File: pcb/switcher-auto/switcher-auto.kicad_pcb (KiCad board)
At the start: 2 copper layers, 129 x 81 mm, 9 parts, among them J1 Conn_02x22_Top_Bottom, J2 Conn_02x22_Top_Bottom, J3 Conn_02x22_Top_Bottom, U1 CD74HC4067SM96, U2 CD74HC4067SM96, U3 CD74HC4067SM96, U4 CD74HC4067SM96, U5 CD74HC4067SM96, U6 CD74HC4067SM96

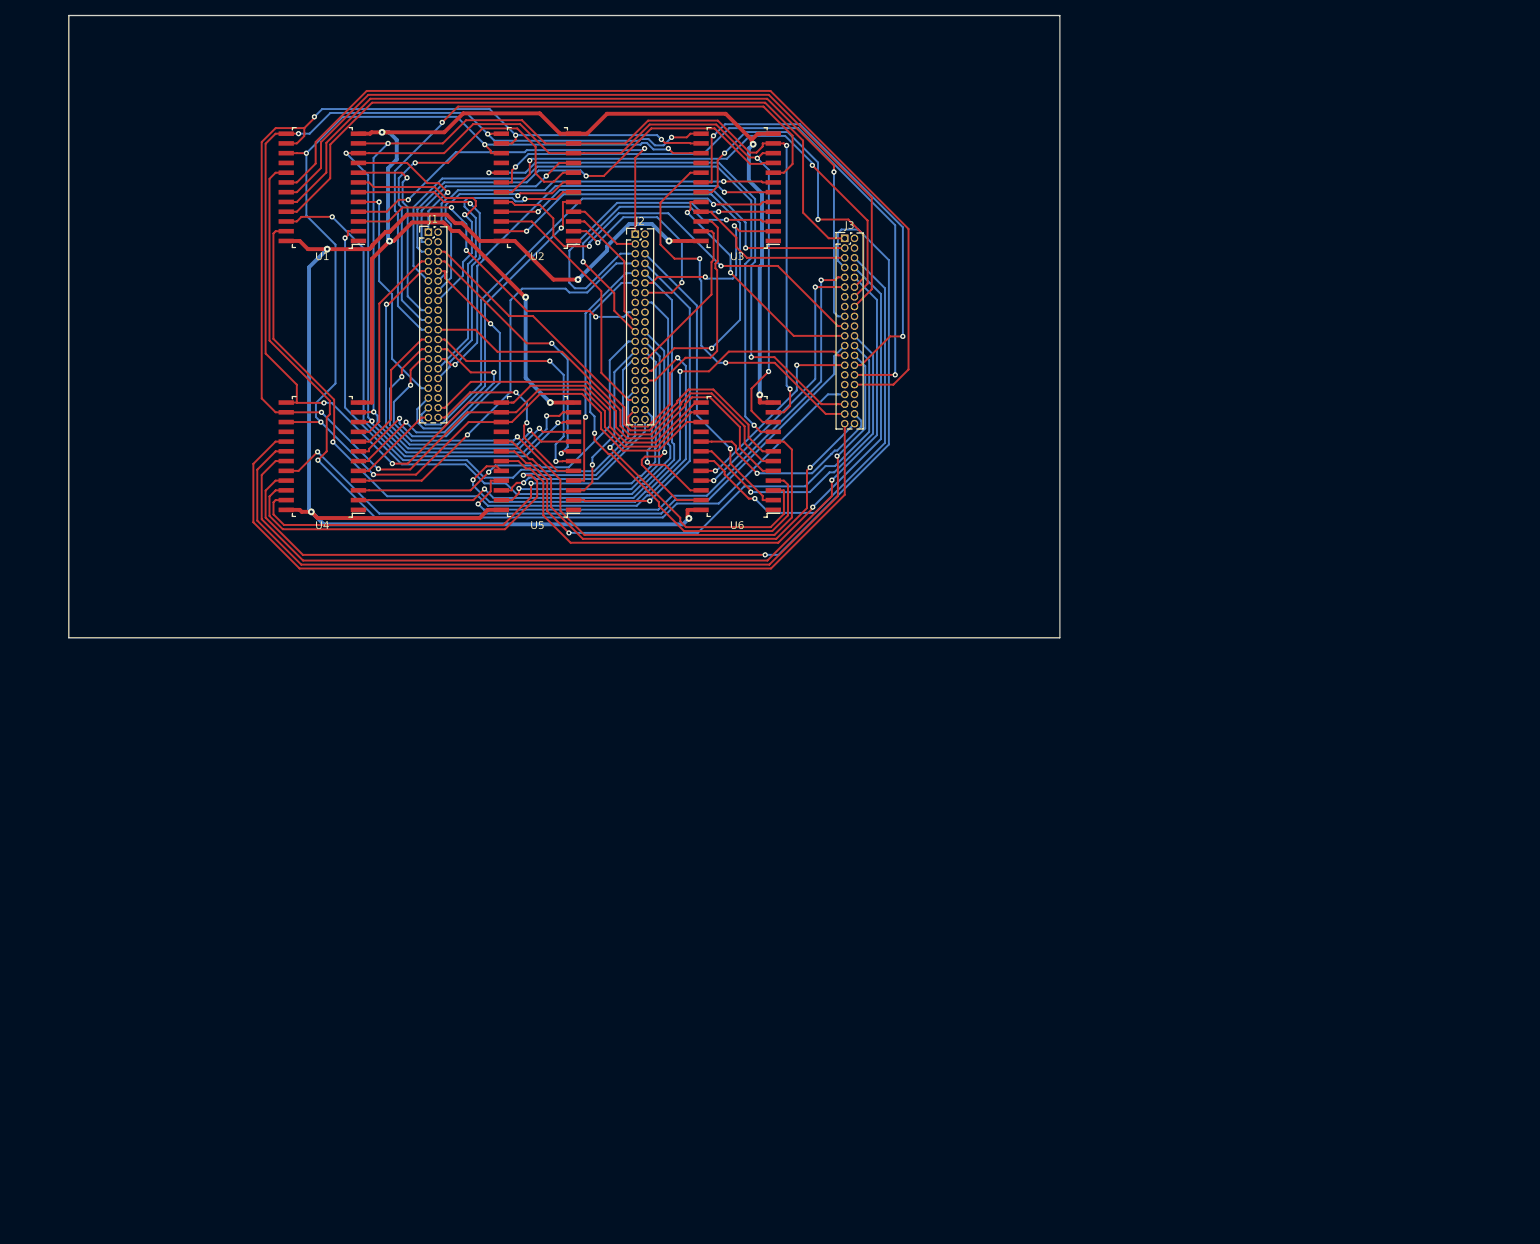
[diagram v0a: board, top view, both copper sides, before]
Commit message: autorouting 2layer switcher
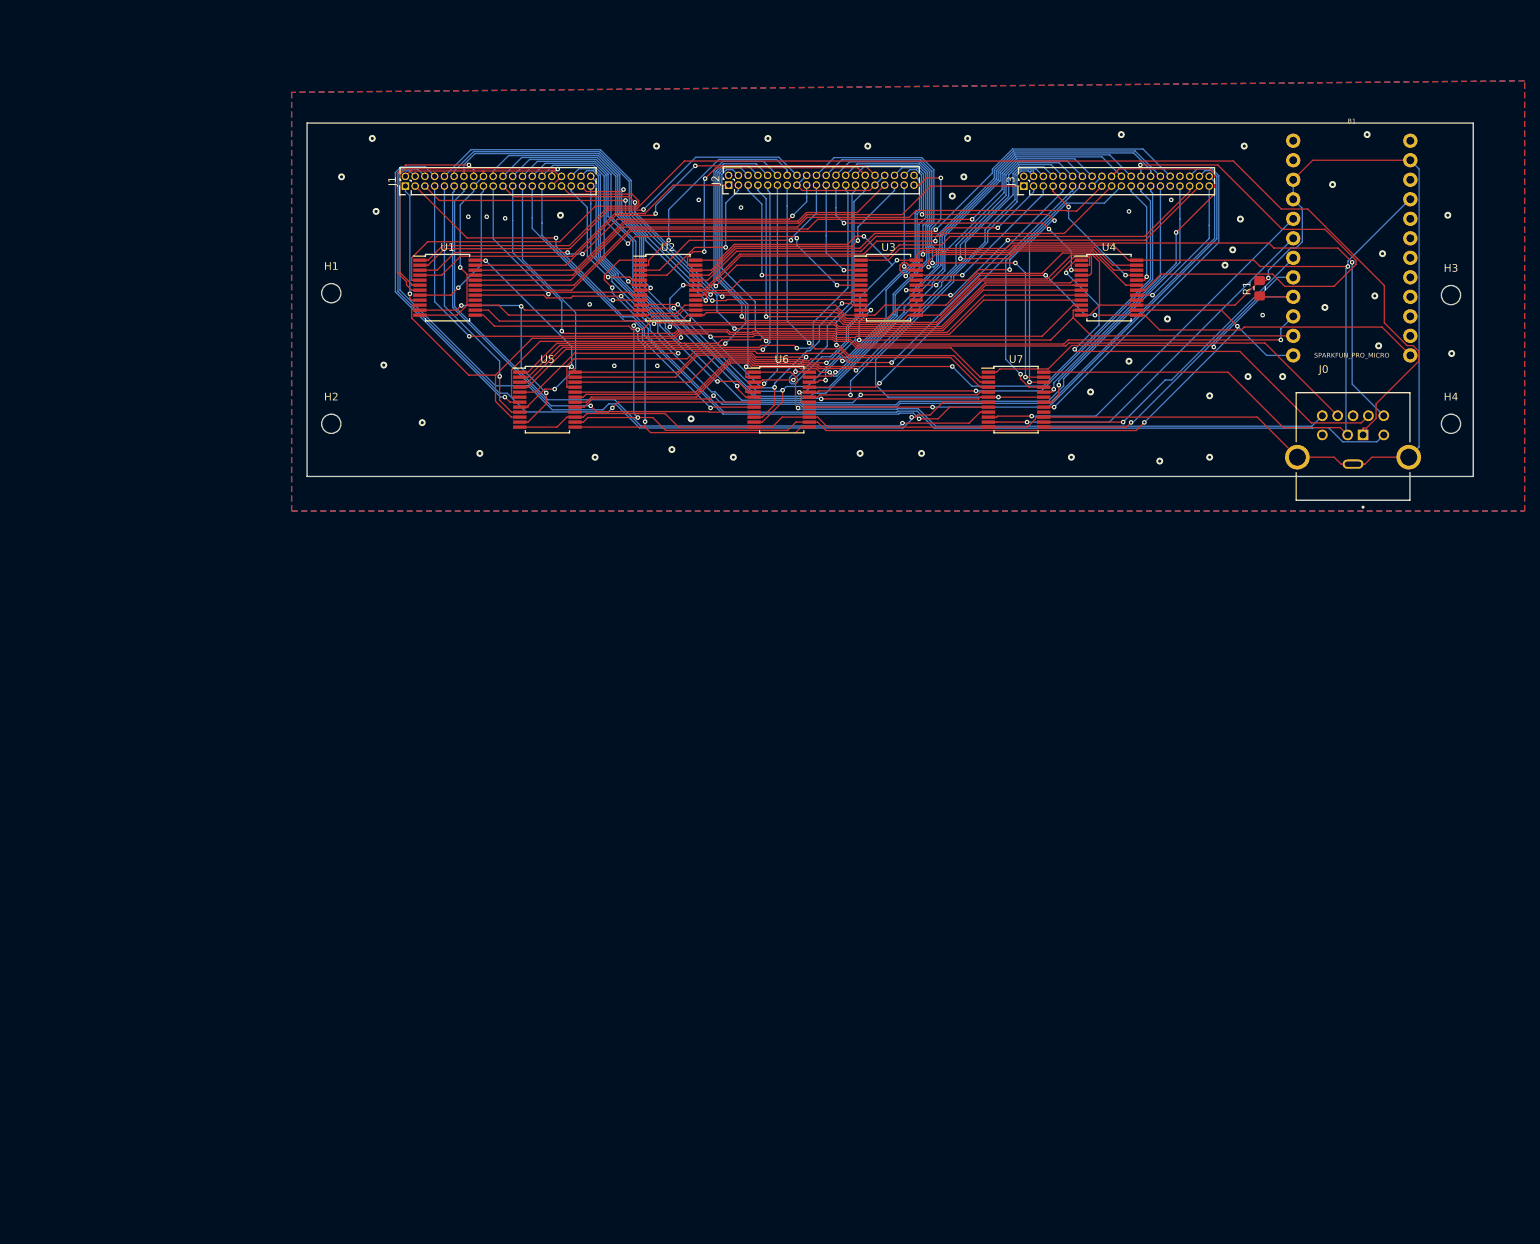
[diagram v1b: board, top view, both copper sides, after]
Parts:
- added B1: SPARKFUN_PRO_MICRO, SparkFun-Boards:SPARKFUN_PRO_MICRO, F.Cu at (210.0, 48.0)
- added H1: MountingHole, MountingHole:MountingHole_2.5mm, F.Cu at (77.2, 55.1)
- added H2: MountingHole, MountingHole:MountingHole_2.5mm, F.Cu at (77.2, 72.1)
- added H3: MountingHole, MountingHole:MountingHole_2.5mm, F.Cu at (222.9, 55.4)
- added H4: MountingHole, MountingHole:MountingHole_2.5mm, F.Cu at (222.9, 72.1)
- added J0: MD-90SM, DIN9:CUI_MD-90SM, F.Cu at (210.2, 77.4)
- added R1: 10K, Resistor_SMD:R_0805_2012Metric_Pad1.20x1.40mm_HandSolder, F.Cu at (198.0, 54.5)
- added U7: CD74HC4067SM96, Package_SO:SSOP-24_5.3x8.2mm_P0.65mm, F.Cu at (166.3, 69.0)
- U1, U2, U3, U4, U5, U6: footprint digikey-footprints:SSOP-24_W5.30mm -> Package_SO:SSOP-24_5.3x8.2mm_P0.65mm
- moved U4 104.9 mm to (178.4, 54.4), turned to 0 degrees
- moved J3 24.3 mm to (167.3, 41.2), turned to 90 degrees
- moved U3 23.3 mm to (149.7, 54.4), turned to 0 degrees
- moved U2 21.1 mm to (121.0, 54.4), turned to 0 degrees
- moved U1 20.5 mm to (92.3, 54.4), turned to 0 degrees
- moved J2 13.7 mm to (128.9, 41.1), turned to 90 degrees
- moved U6 9.88 mm to (135.8, 69.0), turned to 0 degrees
- moved U5 8.10 mm to (105.3, 69.0), turned to 0 degrees
- moved J1 6.70 mm to (86.8, 41.2), turned to 90 degrees
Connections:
- J1 pad 16: /1_GND -> GND
- J1 pad 24: /4_GND -> GND
- J1 pad 32: /3_GND -> GND
- J1 pad 40: /2_GND -> GND
- J1 pad 8: /0_GND -> GND
- J2 pad 16: /6_GND -> GND
- J2 pad 24: /9_GND -> GND
- J2 pad 32: /8_GND -> GND
- J2 pad 40: /7_GND -> GND
- J2 pad 8: /5_GND -> GND
- J3 pad 16: /11_GND -> GND
- J3 pad 24: /14_GND -> GND
- J3 pad 32: /13_GND -> GND
- J3 pad 40: /12_GND -> GND
- J3 pad 8: /10_GND -> GND
- U1 pad 12: /GND -> GND
- U1 pad 15: /~EN -> GND
- U2 pad 12: /GND -> GND
- U2 pad 15: /~EN -> GND
- U3 pad 12: /GND -> GND
- U3 pad 15: /~EN -> GND
- U4 pad 12: /GND -> GND
- U4 pad 15: /~EN -> GND
- U5 pad 12: /GND -> GND
- U5 pad 15: /~EN -> GND
- U6 pad 12: /GND -> GND
- U6 pad 15: /~EN -> GND
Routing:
- net GND: track 0.00 -> 377.5 mm, vias 0 -> 54
- net /GND: track 176.7 -> 0.00 mm, vias 6 -> 0
- net /~EN: track 165.9 -> 0.00 mm, vias 5 -> 0
- net /SEL_BVID: track 0.00 -> 162.6 mm
- net /SEL_GVID: track 0.00 -> 117.8 mm, vias 0 -> 1
- net /10_CVID: track 133.2 -> 17.1 mm, vias 1 -> 2
- net /SEL_LAUD: track 0.00 -> 112.9 mm
- net /2_5V: track 0.00 -> 103.8 mm, vias 0 -> 1
- net /0_5V: track 0.00 -> 92.9 mm, vias 0 -> 1
- net /SEL_RVID: track 0.00 -> 87.6 mm, vias 0 -> 1
- net /14_CVID: track 105.8 -> 19.3 mm, vias 0 -> 1
- net /3_5V: track 0.00 -> 85.7 mm, vias 0 -> 1
- net /SEL_RAUD: track 0.00 -> 79.9 mm, vias 0 -> 1
- net /0_CVID: track 27.3 -> 103.4 mm, vias 0 -> 1
- net /1_5V: track 0.00 -> 75.7 mm, vias 0 -> 1
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- added copper zone on B.Cu, net GND
- added copper zone on F.Cu, net GND
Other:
- board size 129 x 81 mm -> 151.8 x 46 mm
- rule pad_to_mask_clearance: 0.0508 -> 0

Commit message: Updates?
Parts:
- added R2: R, Resistor_SMD:R_1206_3216Metric_Pad1.30x1.75mm_HandSolder, F.Cu at (203.0, 62.0)
- added SW1: SW_Push, Button_Switch_THT:SW_PUSH_6mm, F.Cu at (190.8, 71.8)
- added SW2: SW_Push, Button_Switch_THT:SW_PUSH_6mm, F.Cu at (179.8, 71.8)
- R1: footprint Resistor_SMD:R_0805_2012Metric_Pad1.20x1.40mm_HandSolder -> Resistor_SMD:R_1206_3216Metric_Pad1.30x1.75mm_HandSolder
- moved R1 5.83 mm to (203.0, 57.5), turned to 0 degrees
- moved U7 5.65 mm to (160.7, 69.0)
- moved B1 5.50 mm to (210.0, 42.5), turned to -90 degrees
- moved U6 3.85 mm to (131.9, 69.0)
- moved J2 3.40 mm to (125.5, 41.1)
- moved J3 3.40 mm to (163.9, 41.2)
- moved U2 3.40 mm to (117.6, 54.4)
- moved U4 3.40 mm to (175.0, 54.4)
- moved J1 3.40 mm to (83.4, 41.2)
- moved U1 3.40 mm to (88.9, 54.4)
- moved U3 3.40 mm to (146.3, 54.4)
- moved U5 2.05 mm to (103.2, 69.0)
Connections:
- B1 pad 1: unconnected-(B1-TXO-Pad1) -> /IE
- B1 pad 14: unconnected-(B1-11(MOSI)-Pad14) -> Net-(B1-11(MOSI))
- B1 pad 15: unconnected-(B1-12(MISO)-Pad15) -> Net-(B1-12(MISO))
- B1 pad 2: unconnected-(B1-RXI-Pad2) -> /OE
- B1 pad 9: /SEL_5V -> Net-(B1-*6)
- R1 pad 1: /SEL_5V -> Net-(B1-*6)
- U1 pad 15: GND -> /OE
- U2 pad 15: GND -> /OE
- U3 pad 15: GND -> /OE
- U4 pad 15: GND -> /OE
- U5 pad 15: GND -> /OE
- U6 pad 15: GND -> /OE
- U7 pad 15: GND -> /IE
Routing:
- net GND: track 377.5 -> 20.4 mm, vias 54 -> 108
- net /OE: track 0.00 -> 191.8 mm, vias 0 -> 3
- net /IE: track 0.00 -> 79.5 mm, vias 0 -> 1
- net Net-(B1-*6): track 0.00 -> 45.4 mm, vias 0 -> 1
- net /13_BVID: track 99.8 -> 134.4 mm
- net /S1: track 156.4 -> 190.0 mm, vias 7 -> 6
- net /13_CVID: track 66.5 -> 33.7 mm, vias 1 -> 2
- net Net-(B1-11(MOSI)): track 0.00 -> 32.7 mm
- net Net-(B1-12(MISO)): track 0.00 -> 29.2 mm
- net /11_BVID: track 86.2 -> 115.2 mm, vias 0 -> 2
- net /13_LAUD: track 91.6 -> 118.0 mm, vias 1 -> 2
- net /10_GVID: track 49.4 -> 75.6 mm
- net /12_5V: track 60.9 -> 35.0 mm
- net /12_LAUD: track 79.3 -> 103.8 mm, vias 1 -> 3
- net /11_GVID: track 59.2 -> 82.9 mm, vias 0 -> 1
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
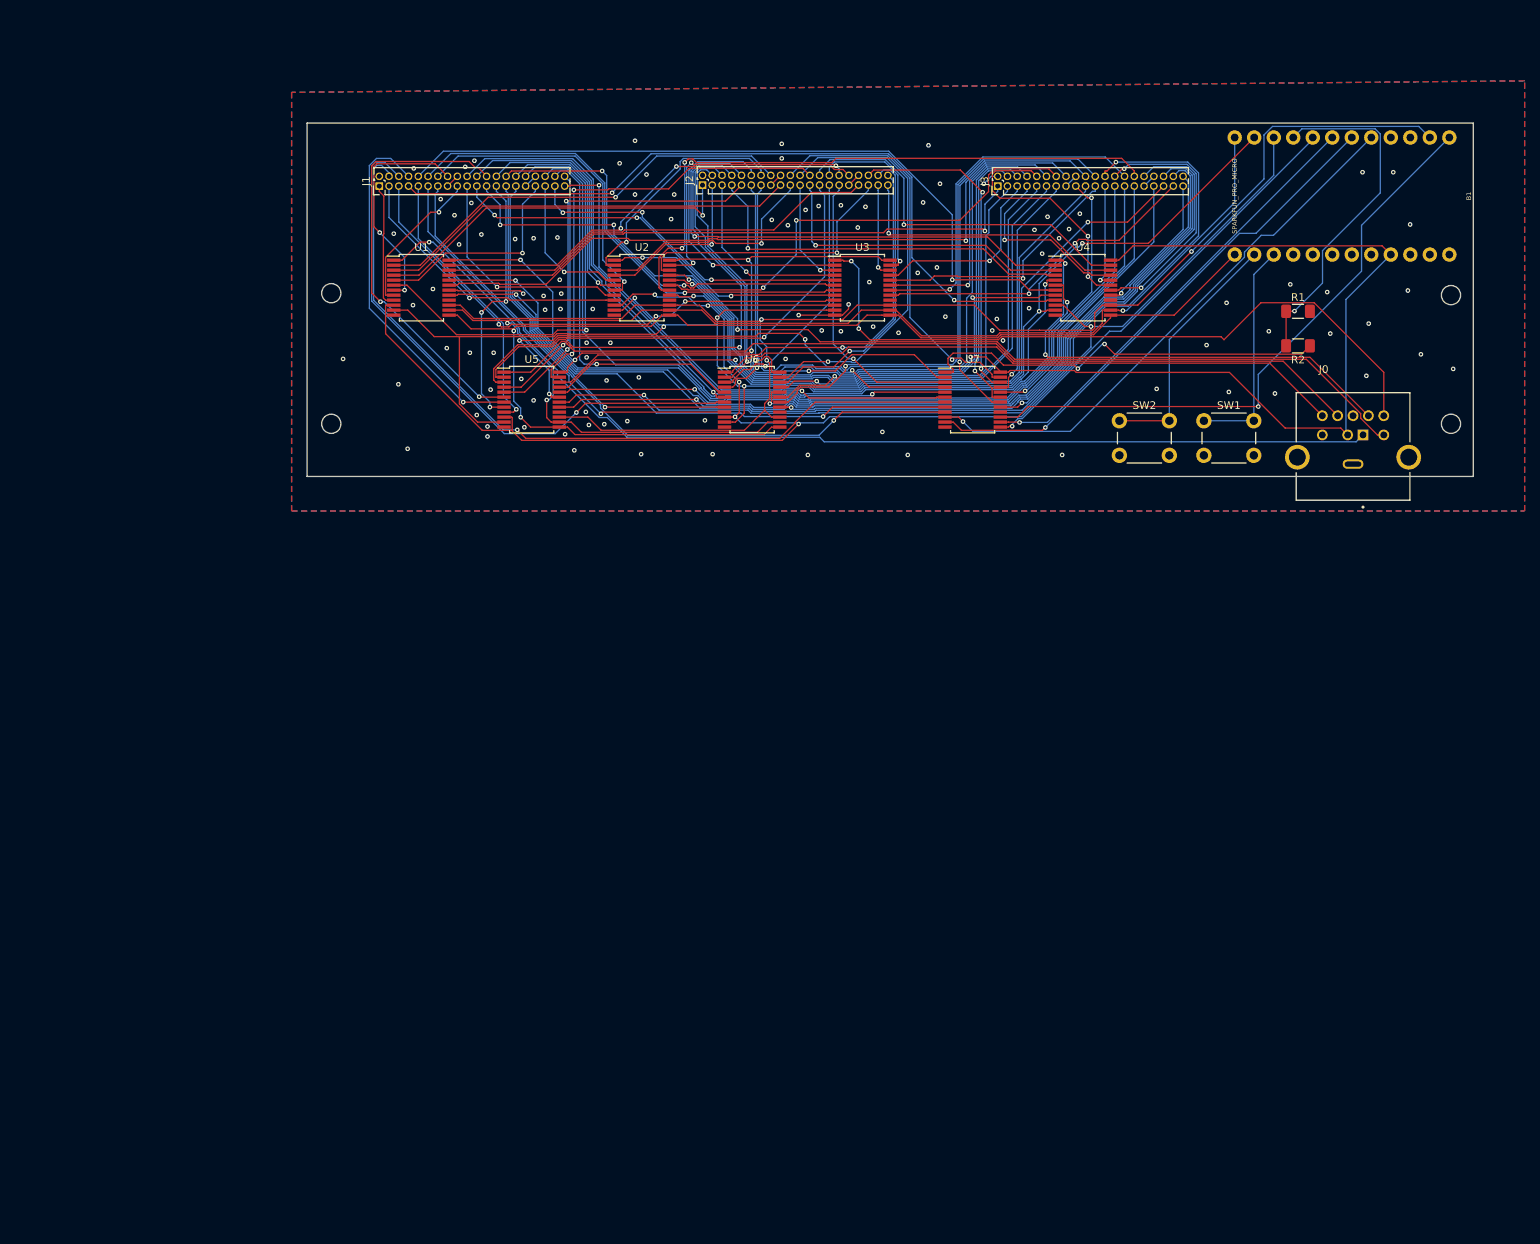
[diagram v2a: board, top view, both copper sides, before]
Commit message: Merge schematics and fix connector mismatch
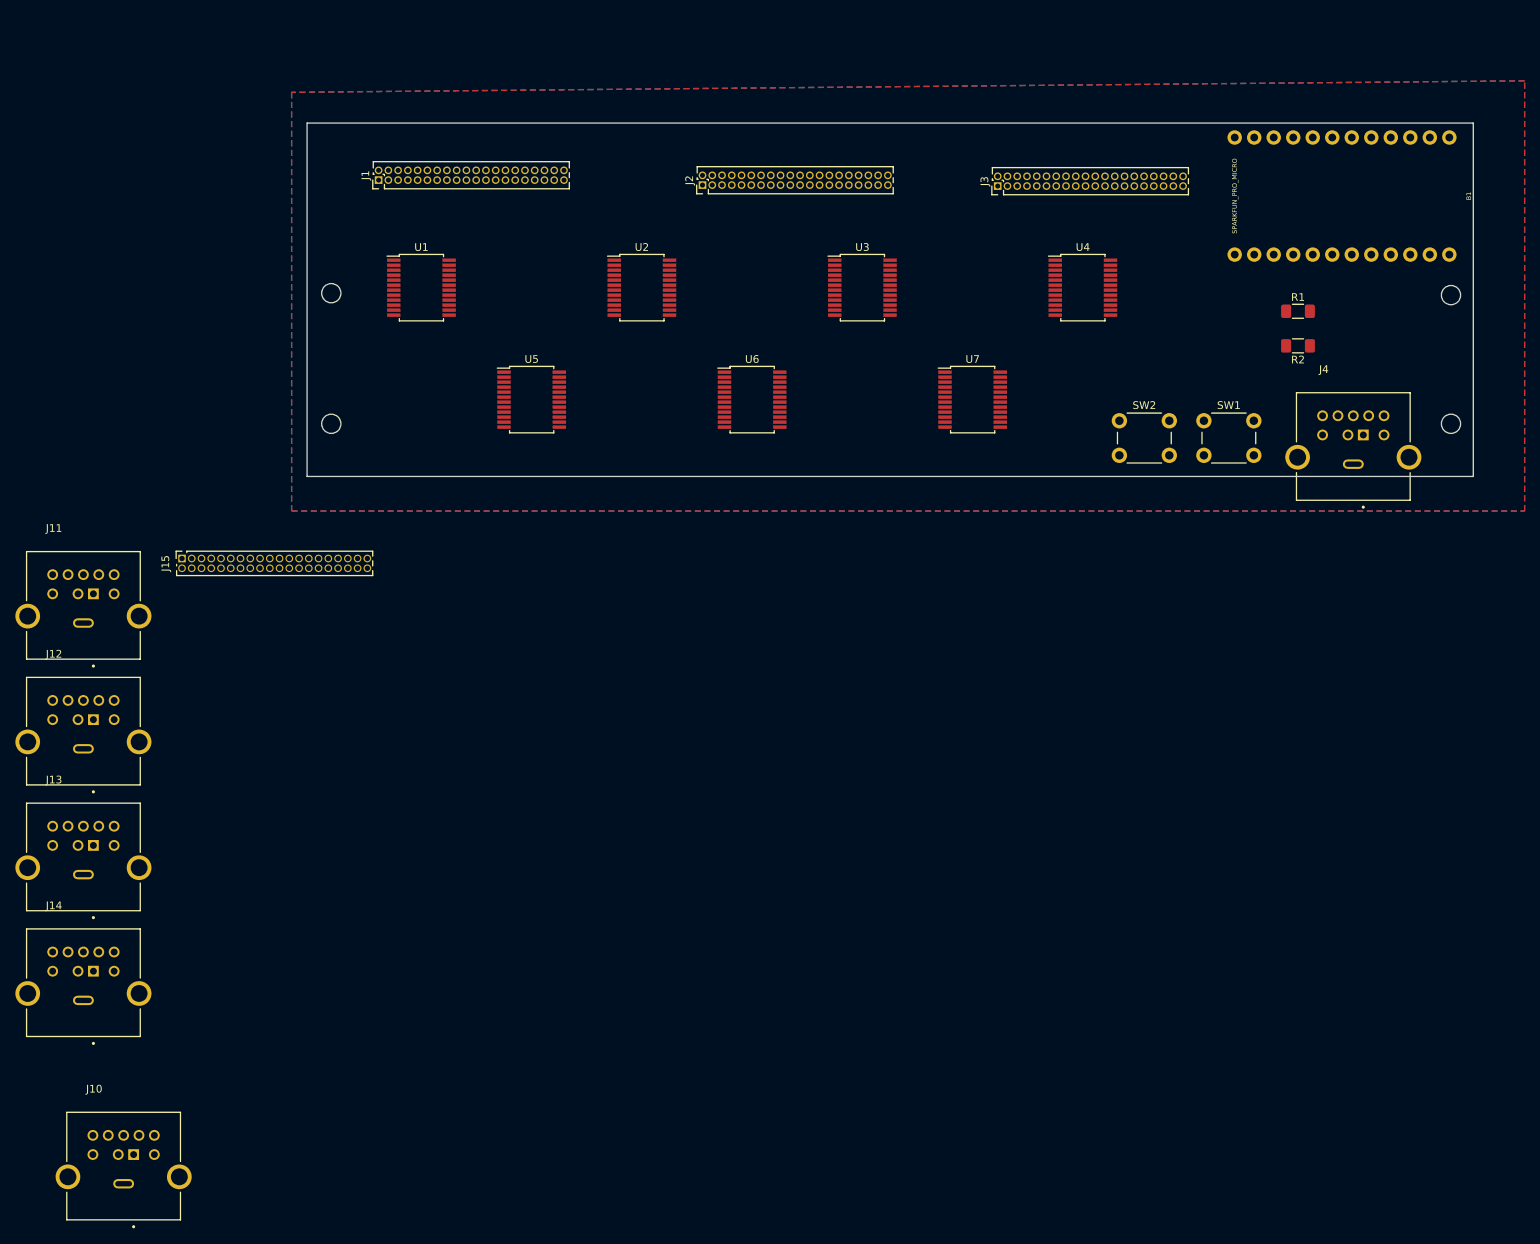
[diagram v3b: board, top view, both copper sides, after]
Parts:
- removed J0: MD-90SM, DIN9:CUI_MD-90SM
- added J10: MD-90SM, DIN9:CUI_MD-90SM, F.Cu at (50.1, 171.1)
- added J11: MD-90SM, DIN9:CUI_MD-90SM, F.Cu at (44.9, 98.1)
- added J12: MD-90SM, DIN9:CUI_MD-90SM, F.Cu at (44.9, 114.5)
- added J13: MD-90SM, DIN9:CUI_MD-90SM, F.Cu at (44.9, 130.8)
- added J14: MD-90SM, DIN9:CUI_MD-90SM, F.Cu at (44.9, 147.2)
- added J15: Conn_02x22_Top_Bottom, Connector_PinSocket_1.27mm:PinSocket_2x20_P1.27mm_Vertical, F.Cu at (57.7, 89.7)
- added J4: MD-90SM, DIN9:CUI_MD-90SM, F.Cu at (210.2, 77.4)
- R1: value 10K -> R
- R2: value R -> 10K
- moved J1 0.78 mm to (83.3, 40.4)
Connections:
- R1 pad 1: Net-(B1-*6) -> /SEL_5V
- R1 pad 2: GND -> Net-(B1-*6)
- R2 pad 1: /SEL_5V -> Net-(B1-*6)
- R2 pad 2: Net-(B1-*6) -> GND
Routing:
- net /VCC: track 248.7 -> 0.00 mm, vias 6 -> 0
- net /S0: track 212.2 -> 0.00 mm, vias 6 -> 0
- net /OE: track 191.8 -> 0.00 mm, vias 3 -> 0
- net /S1: track 190.0 -> 0.00 mm, vias 6 -> 0
- net /S2: track 170.5 -> 0.00 mm, vias 3 -> 0
- net /S3: track 157.8 -> 0.00 mm, vias 2 -> 0
- net /SEL_BVID: track 139.0 -> 0.00 mm, vias 1 -> 0
- net /13_BVID: track 134.4 -> 0.00 mm, vias 1 -> 0
- net /13_LAUD: track 118.0 -> 0.00 mm, vias 2 -> 0
- net /14_BVID: track 117.5 -> 0.00 mm, vias 1 -> 0
- net /11_BVID: track 115.2 -> 0.00 mm, vias 2 -> 0
- net /SEL_LAUD: track 115.0 -> 0.00 mm
- net /SEL_GVID: track 111.0 -> 0.00 mm, vias 2 -> 0
- net /3_CVID: track 106.4 -> 0.00 mm, vias 1 -> 0
- net /2_5V: track 104.0 -> 0.00 mm, vias 1 -> 0
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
